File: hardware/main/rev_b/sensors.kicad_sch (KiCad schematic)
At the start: 16 parts, among them U20 ICM-42688-P, U21 LSM6DSO32TR, U22 LPS22DFTR

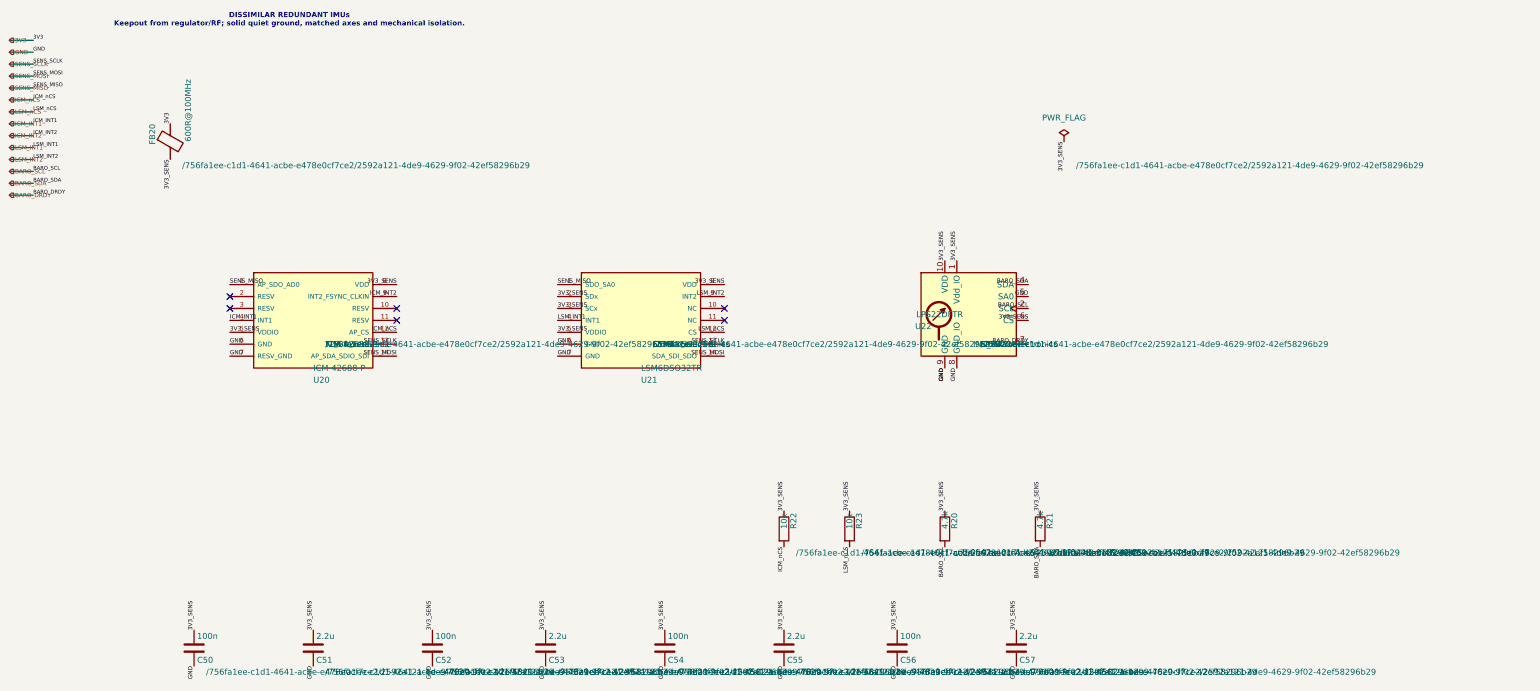
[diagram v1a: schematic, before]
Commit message: build: route and validate rev-b boards
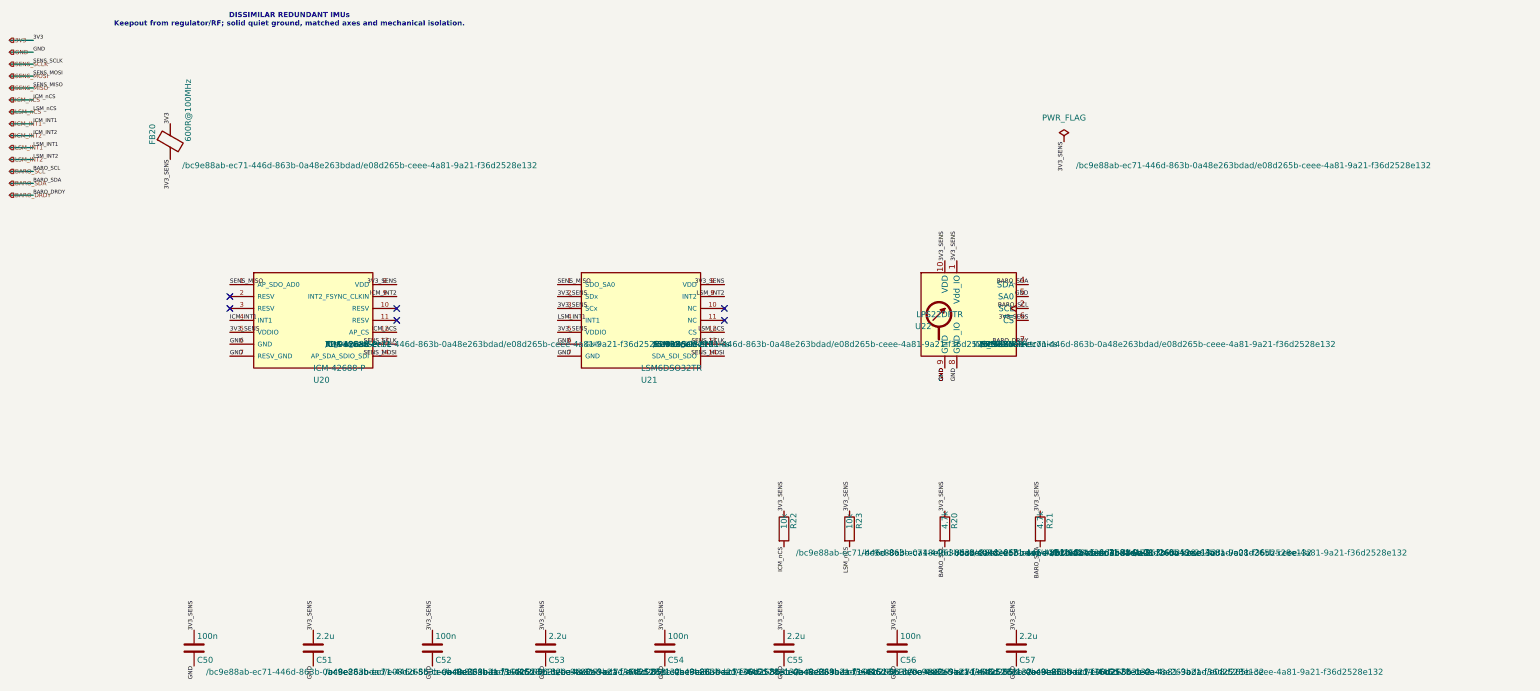
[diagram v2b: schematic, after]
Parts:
- C50, C51, C52, C53, C54, C55, C56, C57, FB20, R20, R21, R22, R23, U20, U21, U22: hierarchy_path /756fa1ee-c1d1-4641-acbe-e478e0cf7ce2/2592a121-4de9-4629-9f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 -> /bc9e88ab-ec71-446d-863b-0a48e263bdad/e08d265b-ceee-4a81-9a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
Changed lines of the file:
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@@
 			)
 		)
-		(property "hierarchy_path" "/756fa1ee-c1d1-4641-acbe-e478e0cf7ce2/2592a121-4de9-4629-9f02-42ef58296b29"
+		(property "hierarchy_path" "/bc9e88ab-ec71-446d-863b-0a48e263bdad/e08d265b-ceee-4a81-9a21-f36d2528e132"
 			(at 57.15 46.9899 0)
 			(effects
@@
 		(instances
 			(project "main_rev_b"
-				(path "/756fa1ee-c1d1-4641-acbe-e478e0cf7ce2/2592a121-4de9-4629-9f02-42ef58296b29"
+				(path "/bc9e88ab-ec71-446d-863b-0a48e263bdad/e08d265b-ceee-4a81-9a21-f36d2528e132"
 					(reference "FB20")
 					(unit 1)
@@
 			)
 		)
-		(property "hierarchy_path" "/756fa1ee-c1d1-4641-acbe-e478e0cf7ce2/2592a121-4de9-4629-9f02-42ef58296b29"
+		(property "hierarchy_path" "/bc9e88ab-ec71-446d-863b-0a48e263bdad/e08d265b-ceee-4a81-9a21-f36d2528e132"
 			(at 87.63 85.0899 0)
 			(effects
@@
 		(instances
 			(project "main_rev_b"
-				(path "/756fa1ee-c1d1-4641-acbe-e478e0cf7ce2/2592a121-4de9-4629-9f02-42ef58296b29"
+				(path "/bc9e88ab-ec71-446d-863b-0a48e263bdad/e08d265b-ceee-4a81-9a21-f36d2528e132"
 					(reference "U20")
 					(unit 1)
@@
 			)
 		)
-		(property "hierarchy_path" "/756fa1ee-c1d1-4641-acbe-e478e0cf7ce2/2592a121-4de9-4629-9f02-42ef58296b29"
+		(property "hierarchy_path" "/bc9e88ab-ec71-446d-863b-0a48e263bdad/e08d265b-ceee-4a81-9a21-f36d2528e132"
 			(at 157.48 85.0899 0)
 			(effects
@@
 		(instances
 			(project "main_rev_b"
-				(path "/756fa1ee-c1d1-4641-acbe-e478e0cf7ce2/2592a121-4de9-4629-9f02-42ef58296b29"
+				(path "/bc9e88ab-ec71-446d-863b-0a48e263bdad/e08d265b-ceee-4a81-9a21-f36d2528e132"
 					(reference "U21")
 					(unit 1)
@@
 			)
 		)
-		(property "hierarchy_path" "/756fa1ee-c1d1-4641-acbe-e478e0cf7ce2/2592a121-4de9-4629-9f02-42ef58296b29"
+		(property "hierarchy_path" "/bc9e88ab-ec71-446d-863b-0a48e263bdad/e08d265b-ceee-4a81-9a21-f36d2528e132"
 			(at 227.33 85.0899 0)
 			(effects
@@
 		(instances
 			(project "main_rev_b"
-				(path "/756fa1ee-c1d1-4641-acbe-e478e0cf7ce2/2592a121-4de9-4629-9f02-42ef58296b29"
+				(path "/bc9e88ab-ec71-446d-863b-0a48e263bdad/e08d265b-ceee-4a81-9a21-f36d2528e132"
 					(reference "U22")
 					(unit 1)
@@
 			)
 		)
-		(property "hierarchy_path" "/756fa1ee-c1d1-4641-acbe-e478e0cf7ce2/2592a121-4de9-4629-9f02-42ef58296b29"
+		(property "hierarchy_path" "/bc9e88ab-ec71-446d-863b-0a48e263bdad/e08d265b-ceee-4a81-9a21-f36d2528e132"
 			(at 222.25 129.5399 0)
 			(effects
@@
 		(instances
 			(project "main_rev_b"
-				(path "/756fa1ee-c1d1-4641-acbe-e478e0cf7ce2/2592a121-4de9-4629-9f02-42ef58296b29"
+				(path "/bc9e88ab-ec71-446d-863b-0a48e263bdad/e08d265b-ceee-4a81-9a21-f36d2528e132"
 					(reference "R20")
 					(unit 1)
@@
 			)
 		)
-		(property "hierarchy_path" "/756fa1ee-c1d1-4641-acbe-e478e0cf7ce2/2592a121-4de9-4629-9f02-42ef58296b29"
+		(property "hierarchy_path" "/bc9e88ab-ec71-446d-863b-0a48e263bdad/e08d265b-ceee-4a81-9a21-f36d2528e132"
 			(at 242.57 129.5399 0)
 			(effects
@@
 		(instances
 			(project "main_rev_b"
-				(path "/756fa1ee-c1d1-4641-acbe-e478e0cf7ce2/2592a121-4de9-4629-9f02-42ef58296b29"
+				(path "/bc9e88ab-ec71-446d-863b-0a48e263bdad/e08d265b-ceee-4a81-9a21-f36d2528e132"
 					(reference "R21")
 					(unit 1)
@@
 			)
 		)
-		(property "hierarchy_path" "/756fa1ee-c1d1-4641-acbe-e478e0cf7ce2/2592a121-4de9-4629-9f02-42ef58296b29"
+		(property "hierarchy_path" "/bc9e88ab-ec71-446d-863b-0a48e263bdad/e08d265b-ceee-4a81-9a21-f36d2528e132"
 			(at 187.96 129.5399 0)
 			(effects
@@
 		(instances
 			(project "main_rev_b"
-				(path "/756fa1ee-c1d1-4641-acbe-e478e0cf7ce2/2592a121-4de9-4629-9f02-42ef58296b29"
+				(path "/bc9e88ab-ec71-446d-863b-0a48e263bdad/e08d265b-ceee-4a81-9a21-f36d2528e132"
 					(reference "R22")
 					(unit 1)
@@
 			)
 		)
-		(property "hierarchy_path" "/756fa1ee-c1d1-4641-acbe-e478e0cf7ce2/2592a121-4de9-4629-9f02-42ef58296b29"
+		(property "hierarchy_path" "/bc9e88ab-ec71-446d-863b-0a48e263bdad/e08d265b-ceee-4a81-9a21-f36d2528e132"
 			(at 201.93 129.5399 0)
 			(effects
@@
 		(instances
 			(project "main_rev_b"
-				(path "/756fa1ee-c1d1-4641-acbe-e478e0cf7ce2/2592a121-4de9-4629-9f02-42ef58296b29"
+				(path "/bc9e88ab-ec71-446d-863b-0a48e263bdad/e08d265b-ceee-4a81-9a21-f36d2528e132"
 					(reference "R23")
 					(unit 1)
@@
 			)
 		)
-		(property "hierarchy_path" "/756fa1ee-c1d1-4641-acbe-e478e0cf7ce2/2592a121-4de9-4629-9f02-42ef58296b29"
+		(property "hierarchy_path" "/bc9e88ab-ec71-446d-863b-0a48e263bdad/e08d265b-ceee-4a81-9a21-f36d2528e132"
 			(at 62.23 154.9399 0)
 			(effects
@@
 		(instances
 			(project "main_rev_b"
-				(path "/756fa1ee-c1d1-4641-acbe-e478e0cf7ce2/2592a121-4de9-4629-9f02-42ef58296b29"
+				(path "/bc9e88ab-ec71-446d-863b-0a48e263bdad/e08d265b-ceee-4a81-9a21-f36d2528e132"
 					(reference "C50")
 					(unit 1)
@@
 			)
 		)
-		(property "hierarchy_path" "/756fa1ee-c1d1-4641-acbe-e478e0cf7ce2/2592a121-4de9-4629-9f02-42ef58296b29"
+		(property "hierarchy_path" "/bc9e88ab-ec71-446d-863b-0a48e263bdad/e08d265b-ceee-4a81-9a21-f36d2528e132"
 			(at 87.63 154.9399 0)
 			(effects
@@
 		(instances
 			(project "main_rev_b"
-				(path "/756fa1ee-c1d1-4641-acbe-e478e0cf7ce2/2592a121-4de9-4629-9f02-42ef58296b29"
+				(path "/bc9e88ab-ec71-446d-863b-0a48e263bdad/e08d265b-ceee-4a81-9a21-f36d2528e132"
 					(reference "C51")
 					(unit 1)
@@
 			)
 		)
-		(property "hierarchy_path" "/756fa1ee-c1d1-4641-acbe-e478e0cf7ce2/2592a121-4de9-4629-9f02-42ef58296b29"
+		(property "hierarchy_path" "/bc9e88ab-ec71-446d-863b-0a48e263bdad/e08d265b-ceee-4a81-9a21-f36d2528e132"
 			(at 113.03 154.9399 0)
 			(effects
@@
 		(instances
 			(project "main_rev_b"
-				(path "/756fa1ee-c1d1-4641-acbe-e478e0cf7ce2/2592a121-4de9-4629-9f02-42ef58296b29"
+				(path "/bc9e88ab-ec71-446d-863b-0a48e263bdad/e08d265b-ceee-4a81-9a21-f36d2528e132"
 					(reference "C52")
 					(unit 1)
@@
 			)
 		)
-		(property "hierarchy_path" "/756fa1ee-c1d1-4641-acbe-e478e0cf7ce2/2592a121-4de9-4629-9f02-42ef58296b29"
+		(property "hierarchy_path" "/bc9e88ab-ec71-446d-863b-0a48e263bdad/e08d265b-ceee-4a81-9a21-f36d2528e132"
 			(at 137.16 154.9399 0)
 			(effects
@@
 		(instances
 			(project "main_rev_b"
-				(path "/756fa1ee-c1d1-4641-acbe-e478e0cf7ce2/2592a121-4de9-4629-9f02-42ef58296b29"
+				(path "/bc9e88ab-ec71-446d-863b-0a48e263bdad/e08d265b-ceee-4a81-9a21-f36d2528e132"
 					(reference "C53")
 					(unit 1)
@@
 			)
 		)
-		(property "hierarchy_path" "/756fa1ee-c1d1-4641-acbe-e478e0cf7ce2/2592a121-4de9-4629-9f02-42ef58296b29"
+		(property "hierarchy_path" "/bc9e88ab-ec71-446d-863b-0a48e263bdad/e08d265b-ceee-4a81-9a21-f36d2528e132"
 			(at 162.56 154.9399 0)
 			(effects
@@
 		(instances
 			(project "main_rev_b"
-				(path "/756fa1ee-c1d1-4641-acbe-e478e0cf7ce2/2592a121-4de9-4629-9f02-42ef58296b29"
+				(path "/bc9e88ab-ec71-446d-863b-0a48e263bdad/e08d265b-ceee-4a81-9a21-f36d2528e132"
 					(reference "C54")
 					(unit 1)
@@
 			)
 		)
-		(property "hierarchy_path" "/756fa1ee-c1d1-4641-acbe-e478e0cf7ce2/2592a121-4de9-4629-9f02-42ef58296b29"
+		(property "hierarchy_path" "/bc9e88ab-ec71-446d-863b-0a48e263bdad/e08d265b-ceee-4a81-9a21-f36d2528e132"
 			(at 187.96 154.9399 0)
 			(effects
@@
 		(instances
 			(project "main_rev_b"
-				(path "/756fa1ee-c1d1-4641-acbe-e478e0cf7ce2/2592a121-4de9-4629-9f02-42ef58296b29"
+				(path "/bc9e88ab-ec71-446d-863b-0a48e263bdad/e08d265b-ceee-4a81-9a21-f36d2528e132"
 					(reference "C55")
 					(unit 1)
@@
 			)
 		)
-		(property "hierarchy_path" "/756fa1ee-c1d1-4641-acbe-e478e0cf7ce2/2592a121-4de9-4629-9f02-42ef58296b29"
+		(property "hierarchy_path" "/bc9e88ab-ec71-446d-863b-0a48e263bdad/e08d265b-ceee-4a81-9a21-f36d2528e132"
 			(at 212.09 154.9399 0)
 			(effects
@@
 		(instances
 			(project "main_rev_b"
-				(path "/756fa1ee-c1d1-4641-acbe-e478e0cf7ce2/2592a121-4de9-4629-9f02-42ef58296b29"
+				(path "/bc9e88ab-ec71-446d-863b-0a48e263bdad/e08d265b-ceee-4a81-9a21-f36d2528e132"
 					(reference "C56")
 					(unit 1)
@@
 			)
 		)
-		(property "hierarchy_path" "/756fa1ee-c1d1-4641-acbe-e478e0cf7ce2/2592a121-4de9-4629-9f02-42ef58296b29"
+		(property "hierarchy_path" "/bc9e88ab-ec71-446d-863b-0a48e263bdad/e08d265b-ceee-4a81-9a21-f36d2528e132"
 			(at 237.49 154.9399 0)
 			(effects
@@
 		(instances
 			(project "main_rev_b"
-				(path "/756fa1ee-c1d1-4641-acbe-e478e0cf7ce2/2592a121-4de9-4629-9f02-42ef58296b29"
+				(path "/bc9e88ab-ec71-446d-863b-0a48e263bdad/e08d265b-ceee-4a81-9a21-f36d2528e132"
 					(reference "C57")
 					(unit 1)
@@
 			)
 		)
-		(property "hierarchy_path" "/756fa1ee-c1d1-4641-acbe-e478e0cf7ce2/2592a121-4de9-4629-9f02-42ef58296b29"
+		(property "hierarchy_path" "/bc9e88ab-ec71-446d-863b-0a48e263bdad/e08d265b-ceee-4a81-9a21-f36d2528e132"
 			(at 247.65 46.9899 0)
 			(effects
@@
 		(instances
 			(project "main_rev_b"
-				(path "/756fa1ee-c1d1-4641-acbe-e478e0cf7ce2/2592a121-4de9-4629-9f02-42ef58296b29"
+				(path "/bc9e88ab-ec71-446d-863b-0a48e263bdad/e08d265b-ceee-4a81-9a21-f36d2528e132"
 					(reference "#FLG20")
 					(unit 1)
